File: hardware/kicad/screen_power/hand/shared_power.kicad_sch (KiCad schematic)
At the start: 12 parts, among them J1 AUX 5V INPUT, Q3 SUP70101EL, Q4 SUP70101EL

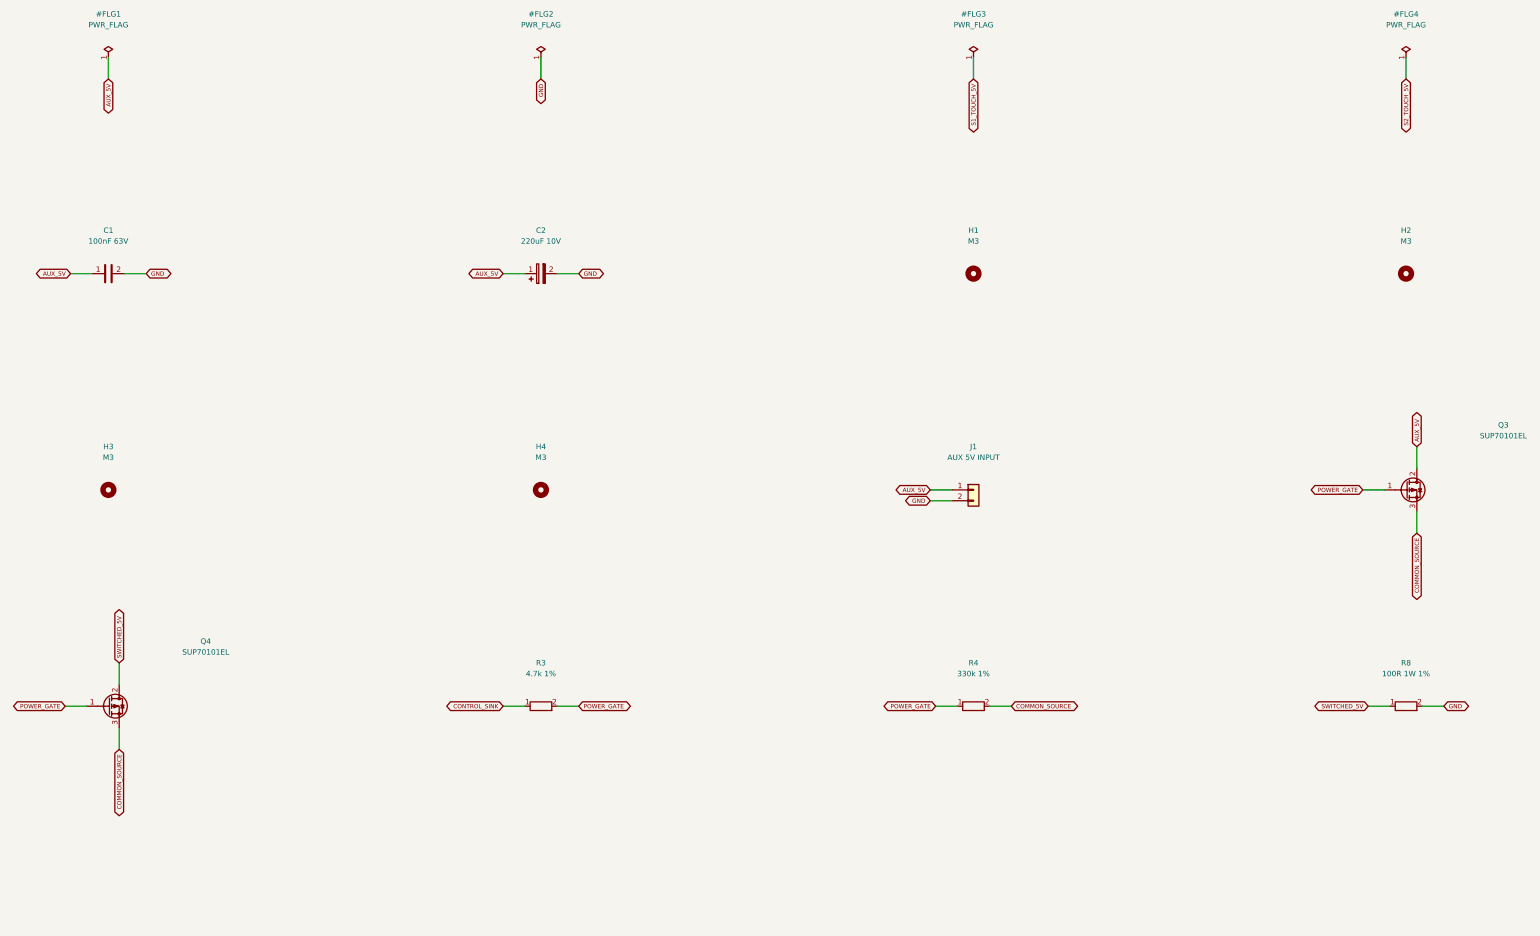
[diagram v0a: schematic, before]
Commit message: feat(hardware): publish screen switching and board refinements
Add the hand-soldered two-layer screen-power board, aligned console connectors, ADC supply isolation, white ring carrier and reviewed manufacturing ZIPs. Integrate GPIO17 ownership with Weston startup and shutdown; retain assembled-system validation as the hardware gate.
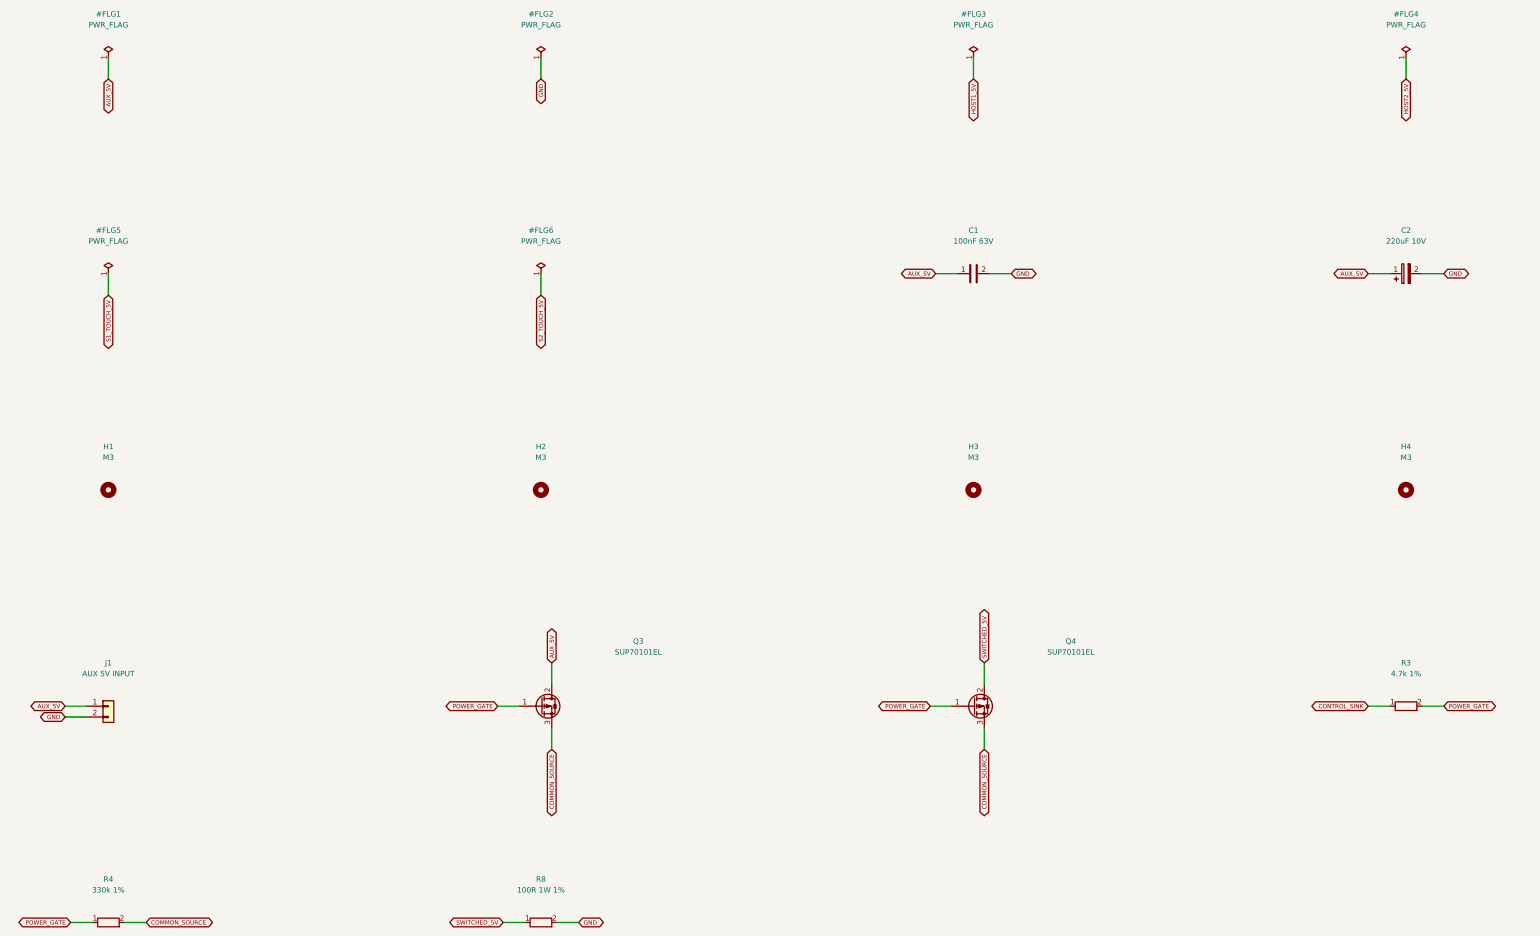
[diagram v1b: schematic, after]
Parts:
- H1, H2, H3, H4: footprint MountingHole:MountingHole_3.2mm_M3 -> MountingHole:MountingHole_3.5mm
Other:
- moved on the sheet: C1, C2, H1, H2, H3, H4, J1, Q3, Q4, R3, R4, R8

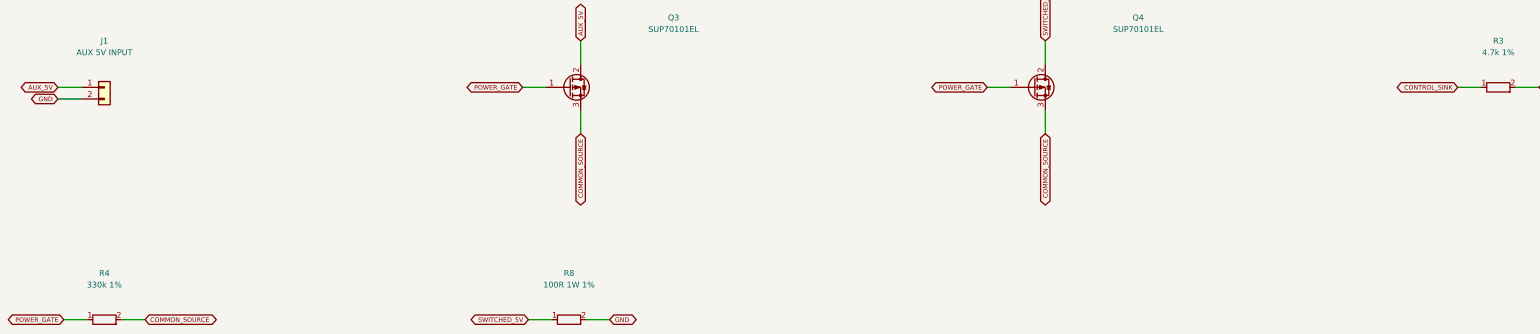
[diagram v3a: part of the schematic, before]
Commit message: fix(hardware): strengthen screen gate drive and finish PCB copper
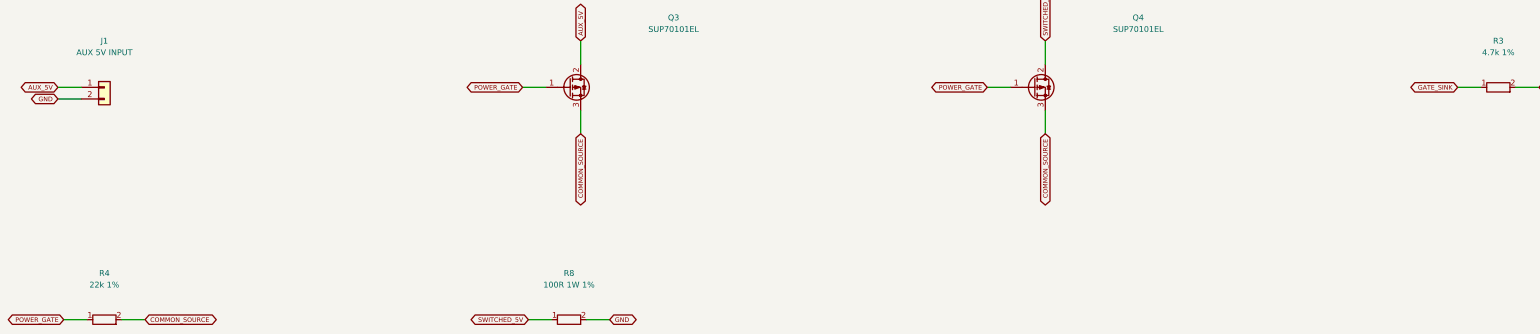
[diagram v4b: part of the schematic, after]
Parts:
- R4: value 330k 1% -> 22k 1%; MPN MFR-25FBF52-330K -> MFR-25FBF52-22K
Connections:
- net CONTROL_SINK renamed GATE_SINK
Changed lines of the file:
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@@
   (title_block
     (title "Segno screen power / hand / shared power")
-    (rev "K prototype")
+    (rev "L prototype")
     (comment 1 "Discrete 5V switch. Host VBUS powers only its own signal relay coil.")
     (comment 2 "Physical verification required before release."))
@@
       (type default))
 )
-  (global_label "CONTROL_SINK"
+  (global_label "GATE_SINK"
     (shape bidirectional)
     (at 346.71 215.9 180)
@@
         (font
           (size 1.27 1.27))))
-    (property "Value" "330k 1%"
+    (property "Value" "22k 1%"
       (at 50.8 259.08 90)
       (effects
@@
           (size 1.27 1.27))
         (hide yes)))
-    (property "MPN" "MFR-25FBF52-330K"
+    (property "MPN" "MFR-25FBF52-22K"
       (at 50.8 266.7 90)
       (effects

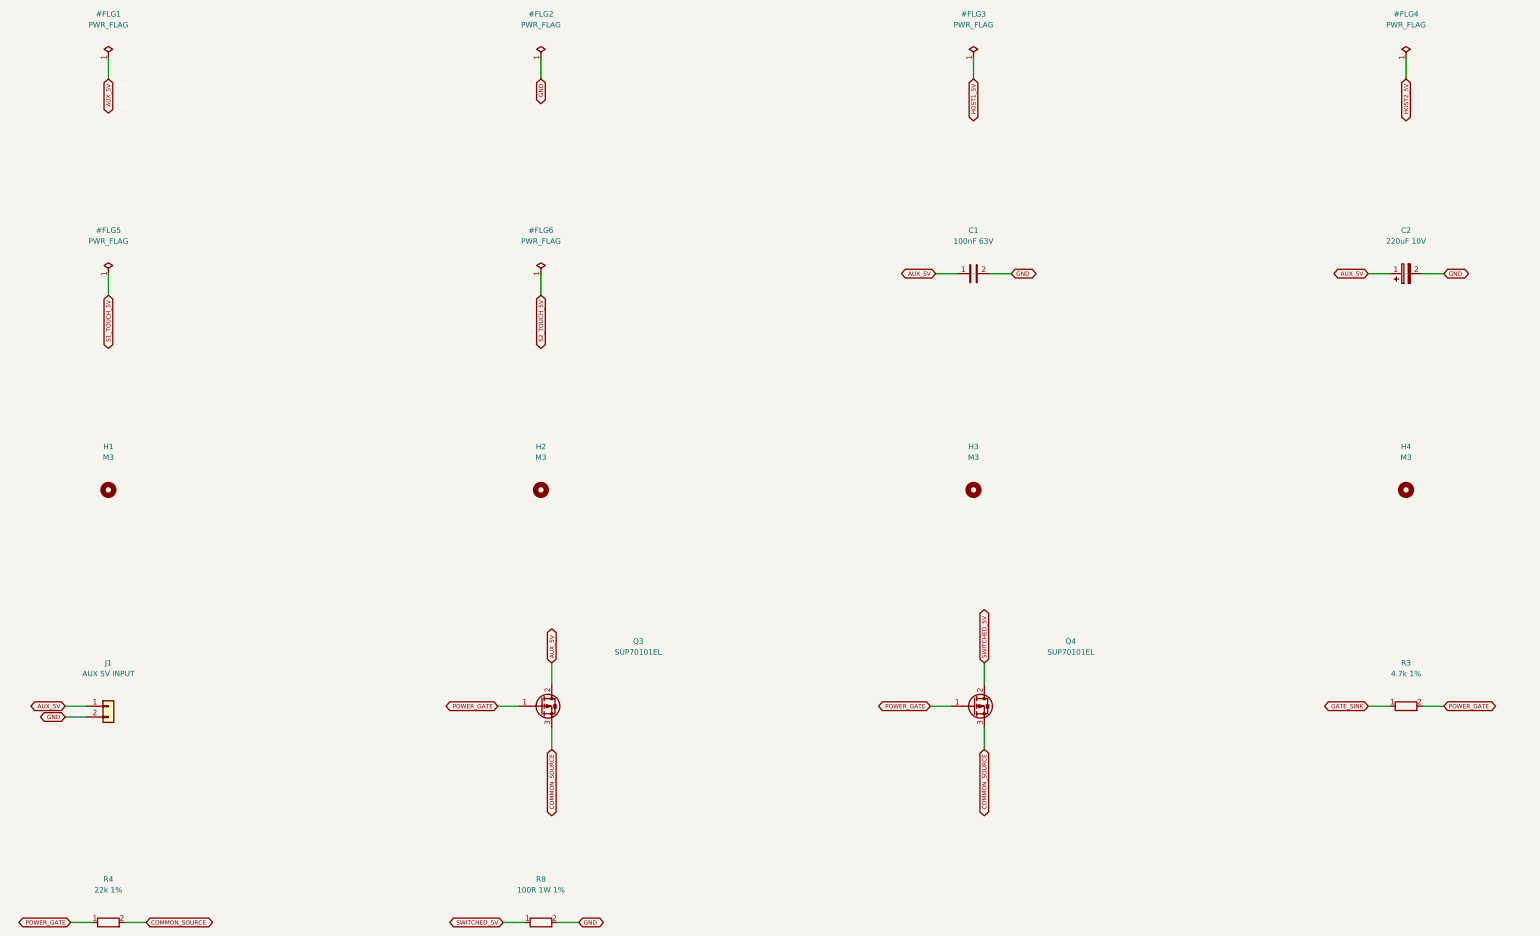
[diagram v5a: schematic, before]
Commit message: feat(hardware): lower screen power cost and finish copper contours
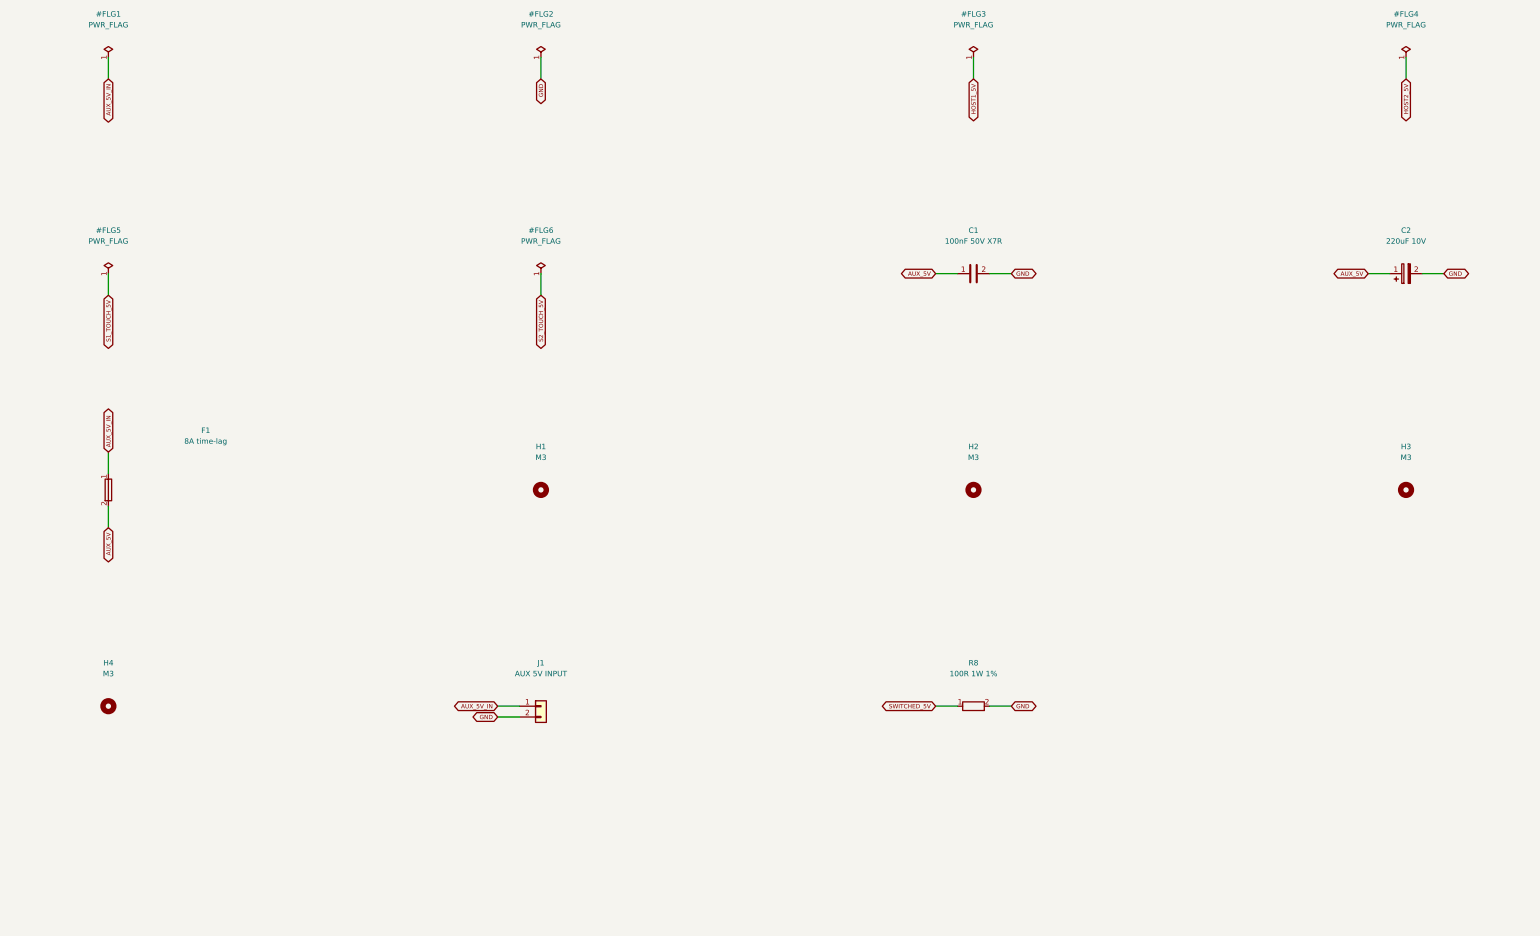
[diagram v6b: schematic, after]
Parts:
- removed Q3, Q4: SUP70101EL, screen_power:TO-220-3_SUP70101EL, symbol screen_symbols:Transistor_FET_Q_PMOS_GDS
- removed R3: 4.7k 1%, Resistor_THT:R_Axial_DIN0207_L6.3mm_D2.5mm_P10.16mm_Horizontal, symbol screen_symbols:Device_R
- removed R4: 22k 1%, Resistor_THT:R_Axial_DIN0207_L6.3mm_D2.5mm_P10.16mm_Horizontal, symbol screen_symbols:Device_R
- added F1: 8A time-lag, screen_power:Fuseholder_Schurter_OGN_0031.8201, symbol screen_symbols:Device_Fuse
- C1: value 100nF 63V -> 100nF 50V X7R; footprint Capacitor_THT:C_Rect_L7.2mm_W2.5mm_P5.00mm -> Capacitor_THT:C_Disc_D7.5mm_W4.4mm_P5.00mm; MPN MKS2C031001A00KSSD -> K104K10X7RF53H5
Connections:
- net AUX_5V: now also F1.2; no longer J1.1 (Pin_1)
- new net AUX_5V_IN: F1.1, J1.1 (Pin_1)
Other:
- moved on the sheet: H1, H2, H3, H4, J1, R8
